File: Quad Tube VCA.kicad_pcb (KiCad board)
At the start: 2 copper layers, 162.6 x 100.3 mm, 226 parts, among them IC1 TL072, IC10 TL072, IC2 LM358, IC3 TL072, IC4 LM358, IC5 TL072, IC6 LM358, IC7 TL072, IC8 LM358, IC9 TL072

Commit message: updates PCB silkscreen
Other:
- board text added: "Vālvs v1.0 PCB Design: Olly Berry"
- board text added: "[HardWired Engineering]"
- board text removed: "HardWired Engineering"
- board text removed: "Quad Tube VCA"
- board text removed: "Vālvs Prototype v0.7 22/01/22 PCB Design: Olly Berry"
- board text removed: "and Émilie Gillet"
- board text removed: "inspired by Ken Stone, L-1"

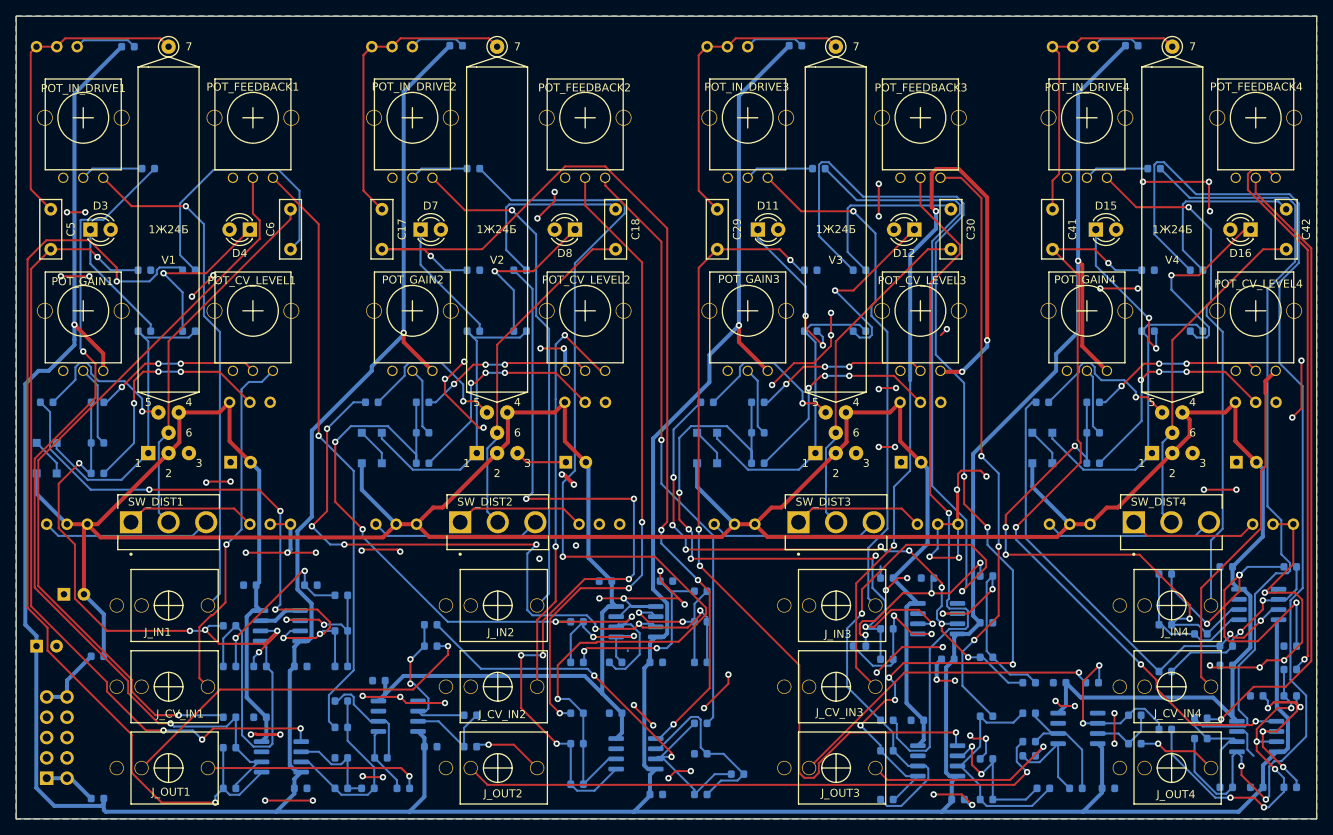
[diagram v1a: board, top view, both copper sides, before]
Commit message: adds keepouts for jack tips
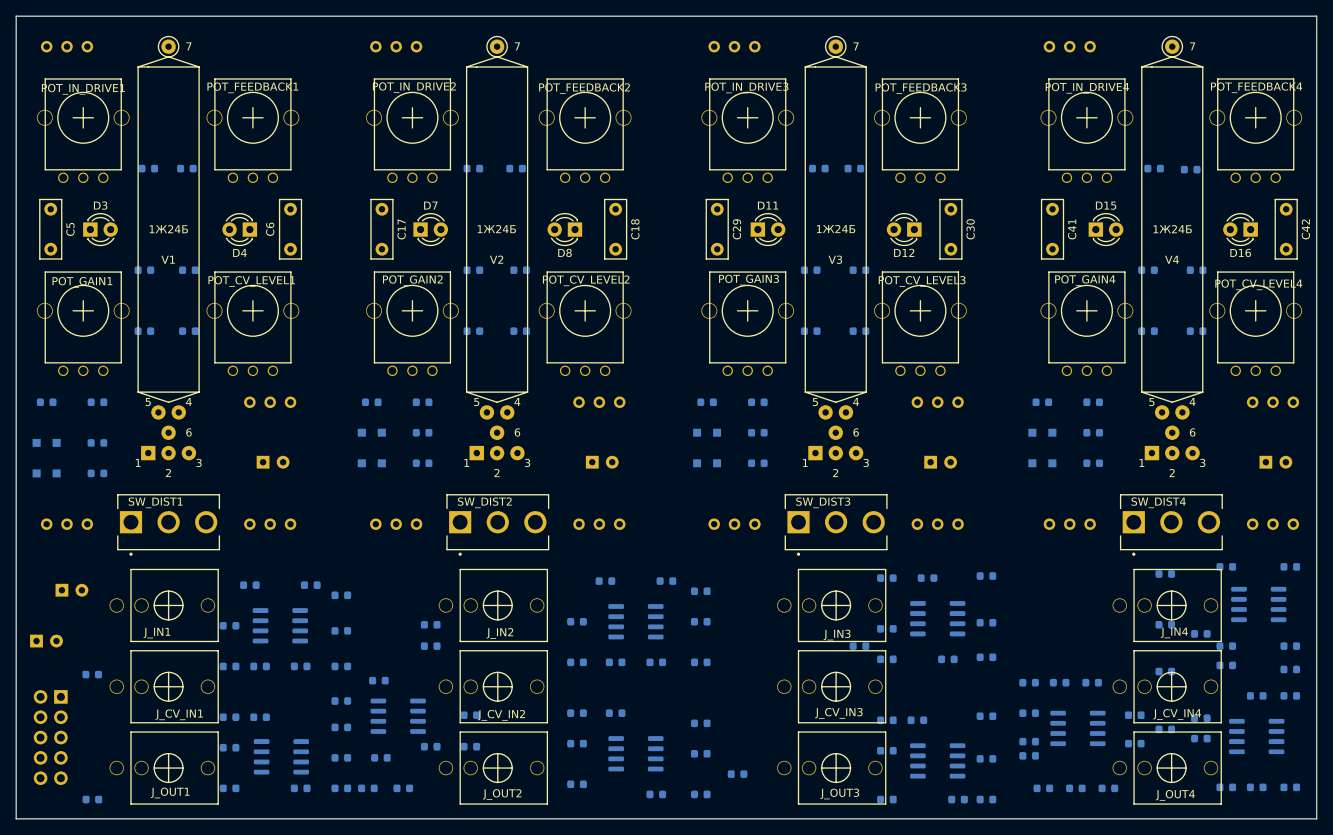
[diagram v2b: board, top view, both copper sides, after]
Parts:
- moved FB2 17.9 mm to (75.6, 142.4)
- moved R66 17.2 mm to (212.9, 63.6)
- moved R26 17.1 mm to (128.5, 63.5)
- moved R46 17.0 mm to (170.8, 63.5)
- moved R6 16.9 mm to (87.4, 63.5)
- moved FB1 15.5 mm to (75.5, 126.7)
- moved JP1 10.3 mm to (71.6, 129.5), turned to 180 degrees
- moved C2 7.67 mm to (71.8, 116.2)
- moved C3 6.77 mm to (68.6, 122.6)
- moved C7 4.06 mm to (96.9, 100.2)
- moved C31 3.68 mm to (180.3, 100.2)
- moved C43 3.68 mm to (222.2, 100.2)
- moved C19 3.30 mm to (138.0, 100.2)
- moved TRIM_CV_INIT1 2.54 mm to (100.3, 92.7)
- moved TRIM_CV_INIT3 2.16 mm to (183.8, 92.7)
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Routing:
- net +12V: track 661.5 -> 0.00 mm, vias 4 -> 0
- net -12V: track 543.7 -> 0.00 mm
- net GND: track 293.9 -> 0.00 mm, vias 84 -> 0
- net Net-(C39-Pad1): track 138.7 -> 0.00 mm, vias 2 -> 0
- net Net-(C27-Pad1): track 138.4 -> 0.00 mm, vias 6 -> 0
- net Net-(C15-Pad2): track 132.2 -> 0.00 mm, vias 2 -> 0
- net Net-(C27-Pad2): track 131.9 -> 0.00 mm, vias 2 -> 0
- net Net-(C17-Pad2): track 124.5 -> 0.00 mm, vias 4 -> 0
- net Net-(C1-Pad1): track 119.8 -> 0.00 mm, vias 2 -> 0
- net Net-(C39-Pad2): track 111.6 -> 0.00 mm
- net Net-(C29-Pad2): track 108.2 -> 0.00 mm, vias 4 -> 0
- net Net-(C1-Pad2): track 108.1 -> 0.00 mm, vias 2 -> 0
- net Net-(J_CV_IN3-Pad3): track 104.0 -> 0.00 mm, vias 4 -> 0
- net Net-(C5-Pad2): track 101.2 -> 0.00 mm, vias 4 -> 0
- net Net-(C15-Pad1): track 100.4 -> 0.00 mm, vias 6 -> 0
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- removed copper zone on B.Cu, net GND
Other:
- board text added: "***RED STRIPE!!"
- board text removed: "red stripe here"

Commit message: lays some long traces
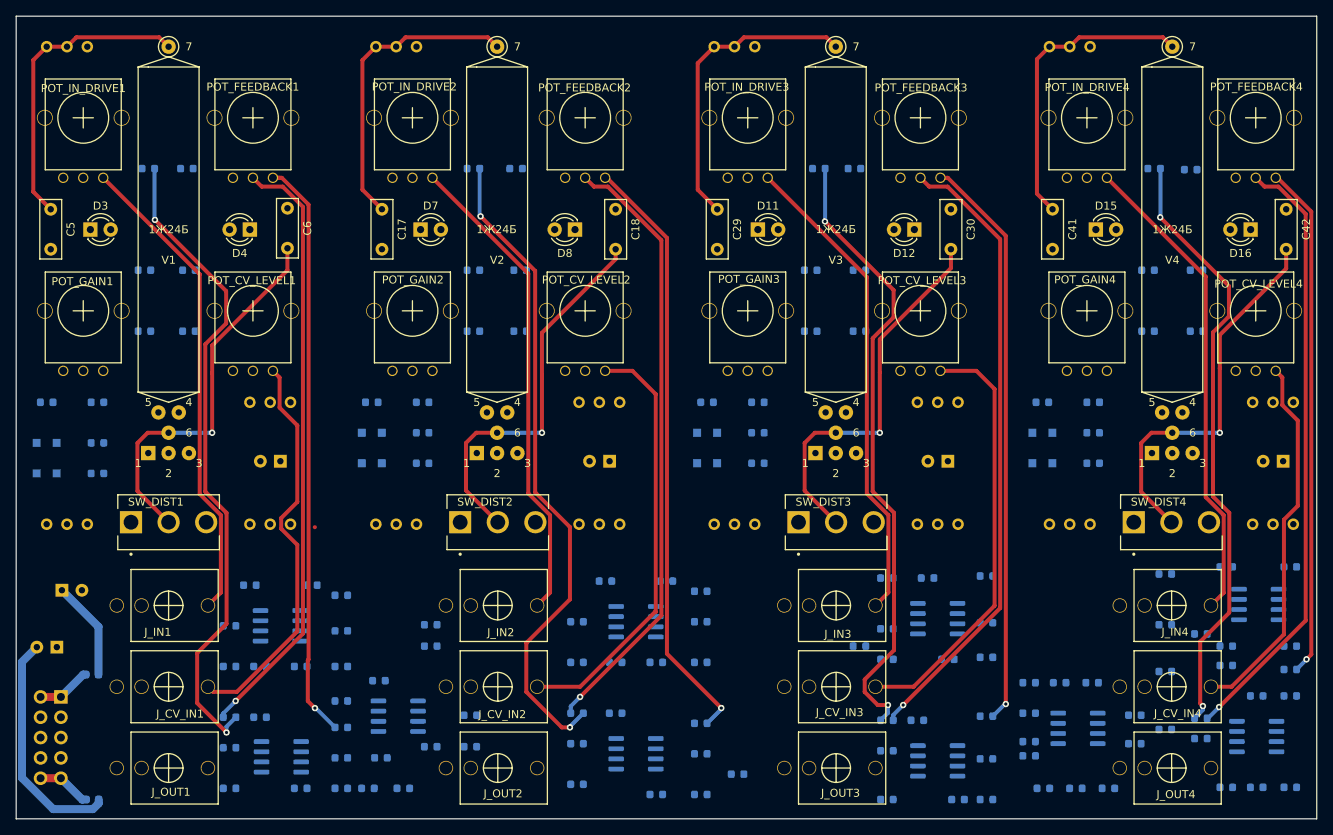
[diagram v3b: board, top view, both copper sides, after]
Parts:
- moved C6 5.14 mm to (99.9, 68.5), turned to 270 degrees
- moved C3 2.65 mm to (71.1, 123.3), turned to 180 degrees
- moved C7 2.16 mm to (99.1, 100.1), turned to 180 degrees
- moved C19 2.16 mm to (140.2, 100.1), turned to 180 degrees
- moved C31 2.16 mm to (182.5, 100.1), turned to 180 degrees
- moved C43 2.16 mm to (224.4, 100.1), turned to 180 degrees
- turned C23 to 180 degrees
- turned C40 to 0 degrees
- turned R19 to 180 degrees
- turned R85 to 180 degrees
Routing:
- net Net-(C15-Pad2): track 0.00 -> 82.1 mm, vias 0 -> 2
- net Net-(C1-Pad2): track 0.00 -> 81.8 mm, vias 0 -> 2
- net Net-(POT_FEEDBACK3-Pad2): track 0.00 -> 78.8 mm, vias 0 -> 1
- net Net-(C27-Pad2): track 0.00 -> 78.6 mm, vias 0 -> 2
- net Net-(POT_FEEDBACK2-Pad2): track 0.00 -> 76.6 mm, vias 0 -> 1
- net Net-(POT_FEEDBACK4-Pad2): track 0.00 -> 76.3 mm, vias 0 -> 1
- net Net-(C39-Pad2): track 0.00 -> 76.0 mm, vias 0 -> 2
- net Net-(POT_FEEDBACK1-Pad2): track 0.00 -> 75.7 mm, vias 0 -> 1
- net Net-(POT_FEEDBACK2-Pad3): track 0.00 -> 75.3 mm, vias 0 -> 1
- net Net-(POT_FEEDBACK1-Pad3): track 0.00 -> 73.6 mm, vias 0 -> 1
- net Net-(POT_FEEDBACK3-Pad3): track 0.00 -> 72.0 mm, vias 0 -> 1
- net Net-(POT_FEEDBACK4-Pad3): track 0.00 -> 64.2 mm, vias 0 -> 1
- net Net-(J_IN3-Pad3): track 0.00 -> 60.4 mm
- net Net-(J_IN2-Pad3): track 0.00 -> 60.2 mm
- net Net-(J_IN1-Pad3): track 0.00 -> 60.2 mm
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
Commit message: connects -12V
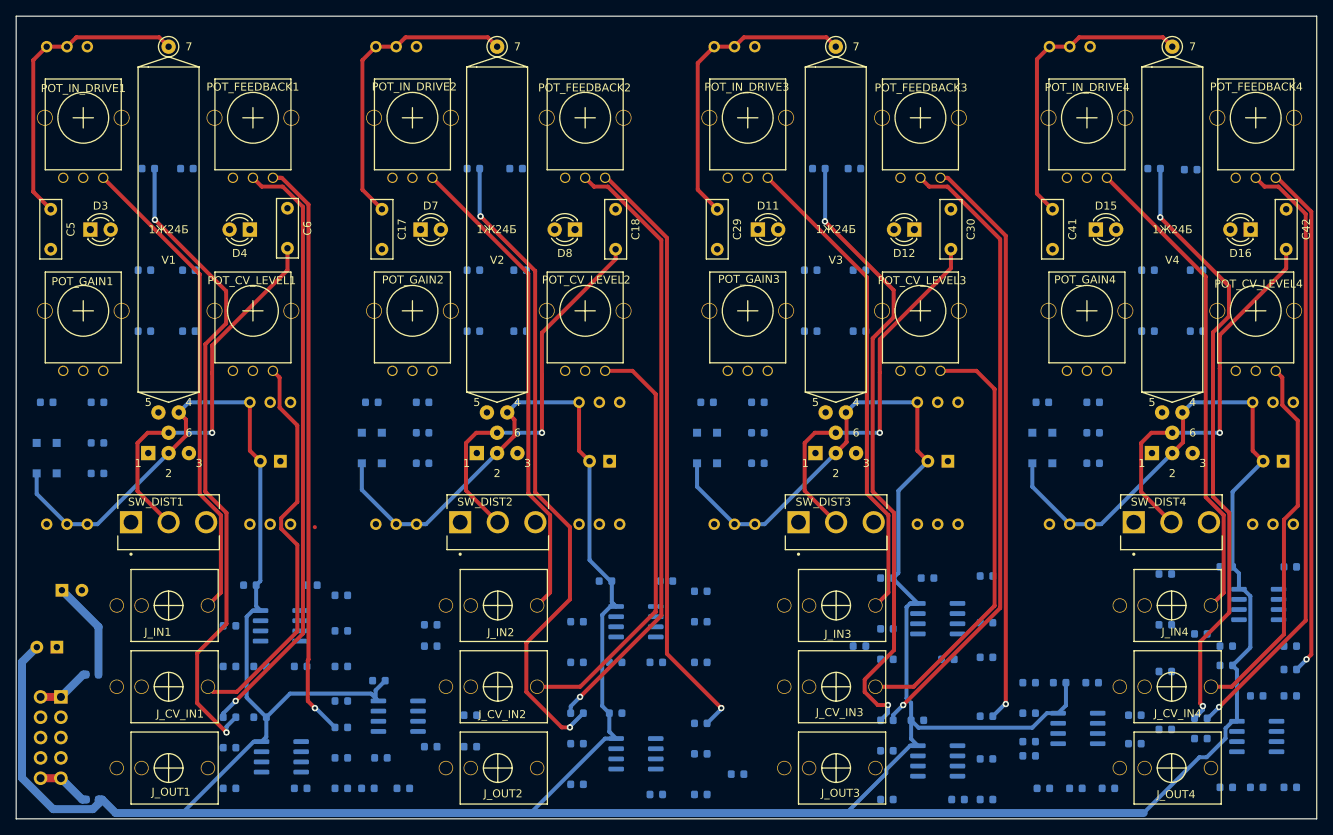
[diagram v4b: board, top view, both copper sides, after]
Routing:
- net -12V: track 29.1 -> 609.7 mm

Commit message: connects +12V
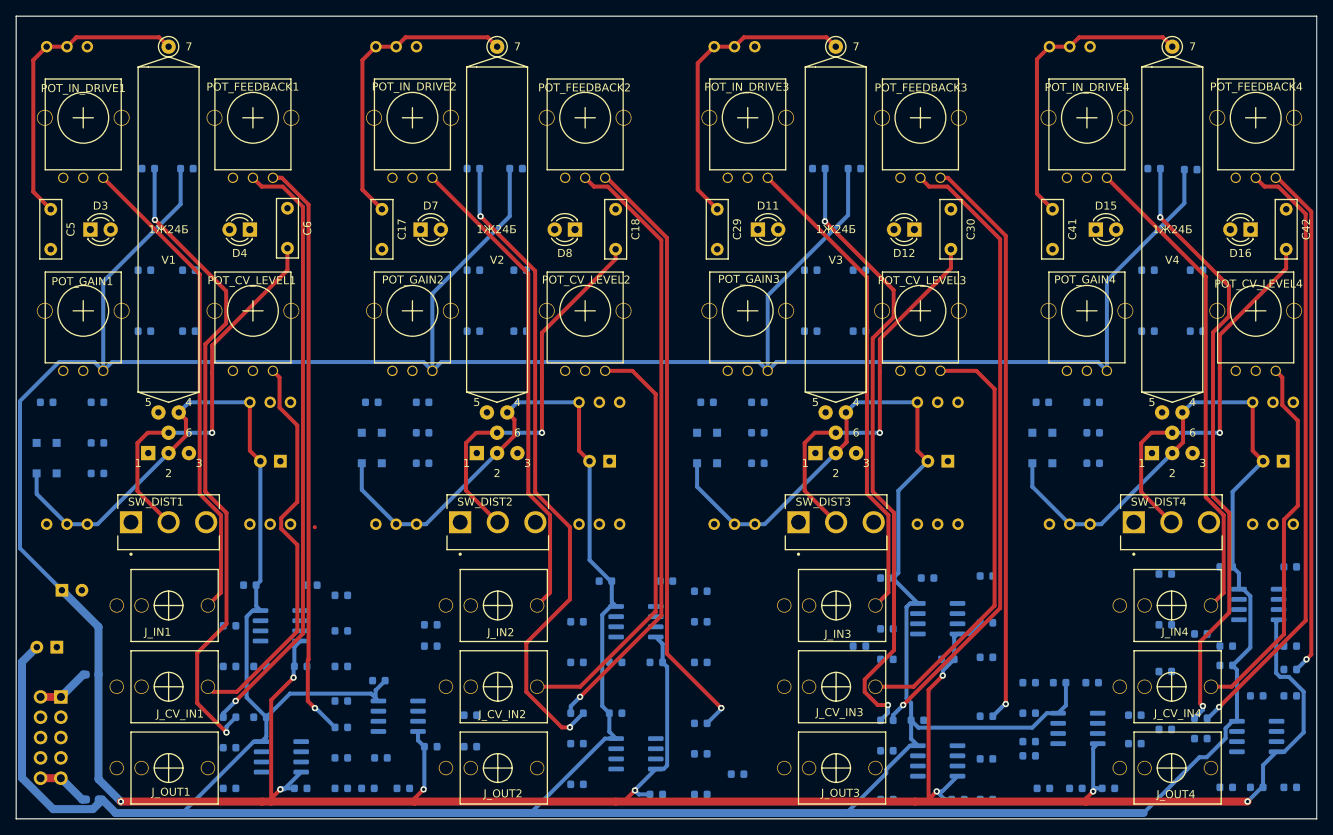
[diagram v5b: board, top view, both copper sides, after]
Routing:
- net +12V: track 12.4 -> 593.0 mm, vias 0 -> 9

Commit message: first GND pour
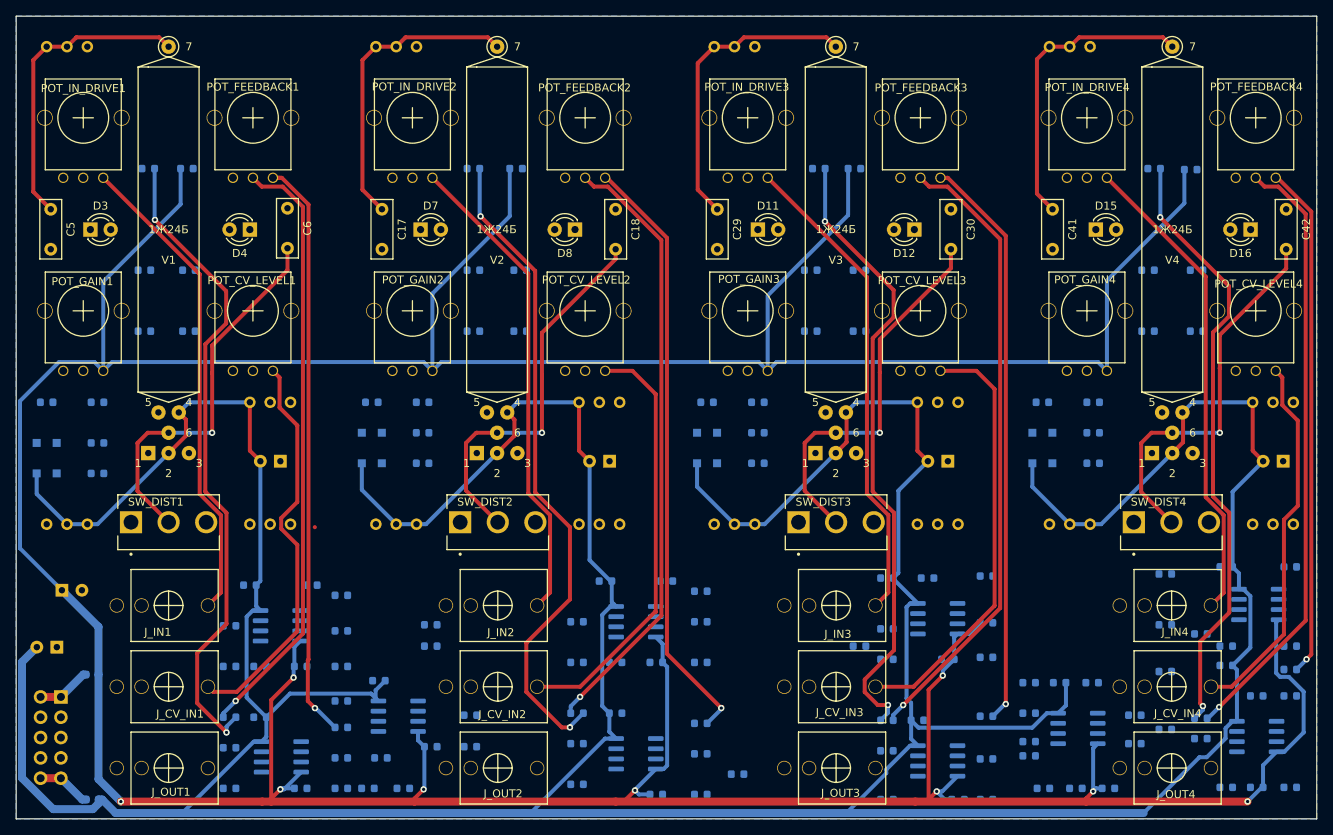
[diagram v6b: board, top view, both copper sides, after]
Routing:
- added copper zone on B.Cu, net GND
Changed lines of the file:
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@@
+    )
+  )
+  (zone (net 3) (net_name GND) (layer B.Cu) (hatch edge 0.508)
+    (connect_pads (clearance 0.508))
+    (min_thickness 0.254)
+    (fill yes (arc_segments 32) (thermal_gap 0.508) (thermal_bridge_width 0.508))
+    (polygon
+      (pts
+        (xy 228.6 144.78) (xy 66.04 144.78) (xy 66.04 44.45) (xy 228.6 44.45)
+      )
     )
   )

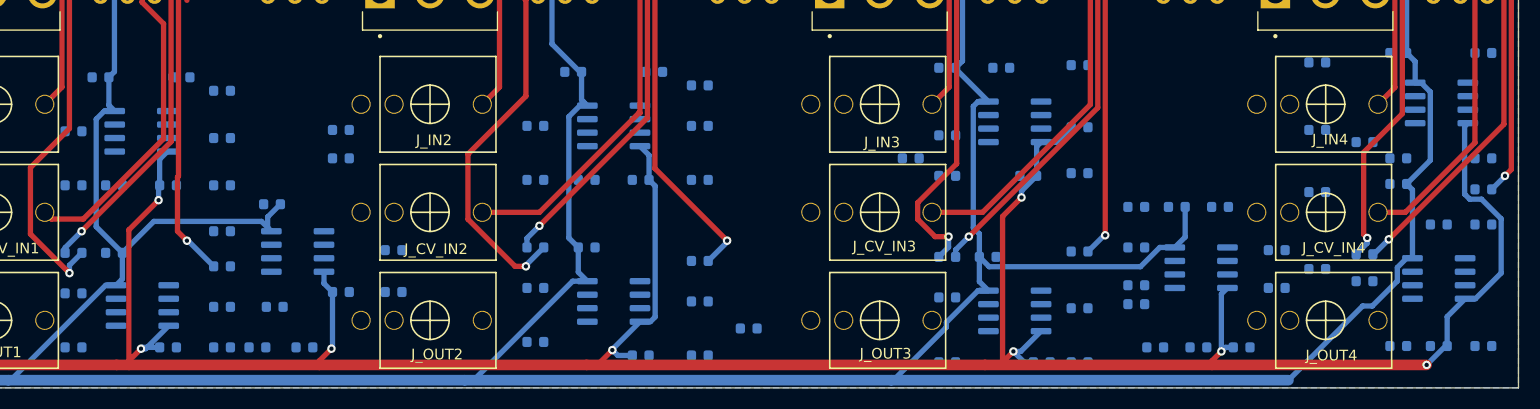
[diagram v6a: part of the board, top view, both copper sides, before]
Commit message: op amp traces [WIP]
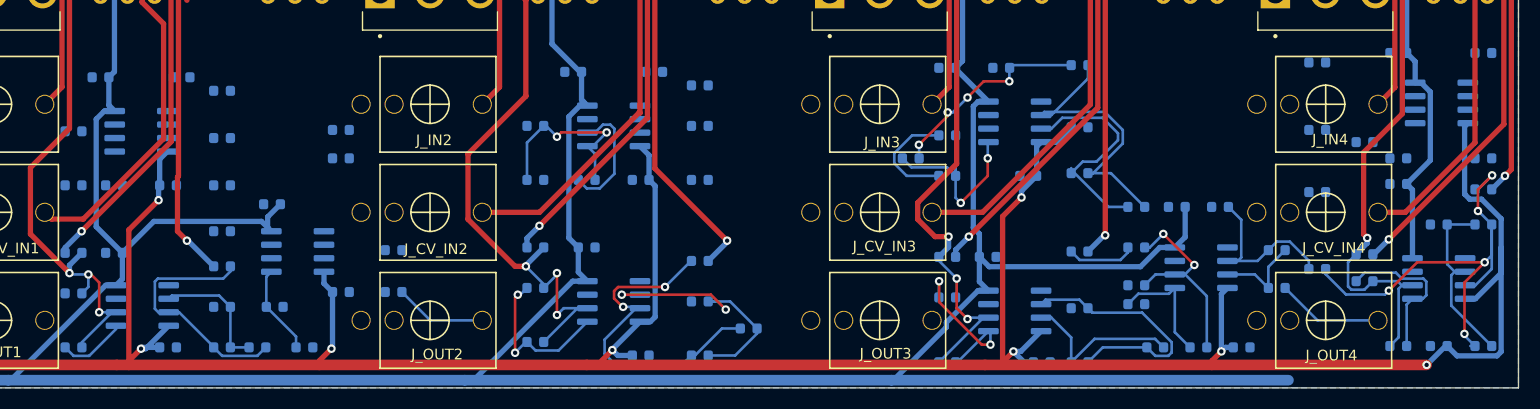
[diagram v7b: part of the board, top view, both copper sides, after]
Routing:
- net Net-(C40-Pad2): track 0.00 -> 46.1 mm, vias 0 -> 5
- net Net-(C16-Pad2): track 0.00 -> 32.4 mm, vias 0 -> 2
- net Net-(C32-Pad1): track 0.00 -> 28.0 mm
- net Net-(C16-Pad1): track 0.00 -> 25.6 mm, vias 0 -> 2
- net Net-(C28-Pad1): track 0.00 -> 24.0 mm
- net Net-(C4-Pad2): track 0.00 -> 23.2 mm
- net Net-(C33-Pad2): track 0.00 -> 22.8 mm, vias 0 -> 2
- net Net-(C28-Pad2): track 0.00 -> 22.3 mm
- net Net-(C32-Pad2): track 0.00 -> 22.1 mm
- net Net-(IC10-Pad2): track 0.00 -> 20.5 mm, vias 0 -> 2
- net Net-(C38-Pad1): track 0.00 -> 19.6 mm, vias 0 -> 4
- net Net-(C21-Pad2): track 0.00 -> 18.1 mm, vias 0 -> 2
- net Net-(C27-Pad2): track 78.6 -> 95.8 mm, vias 2 -> 4
- net Net-(C39-Pad2): track 76.0 -> 93.2 mm
- net Net-(C15-Pad2): track 82.1 -> 99.2 mm, vias 2 -> 4
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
